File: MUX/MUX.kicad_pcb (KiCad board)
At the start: 4 copper layers, 364 x 203 mm, 139 parts, among them P1 Conn_02x36_Top_Bottom, P2 DB9_Male, P3 DB9_Male, P4 DB9_Male, P5 DB9_Male

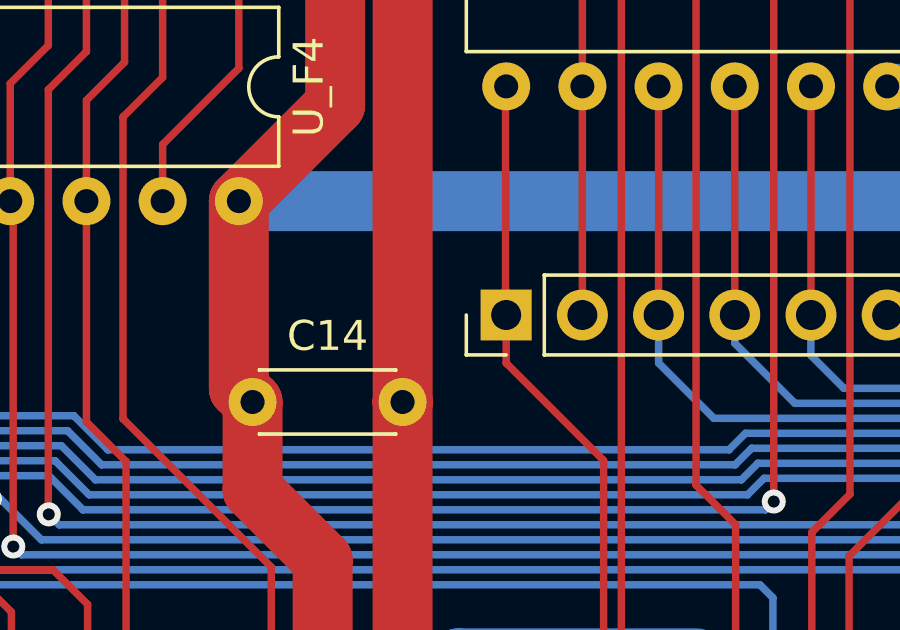
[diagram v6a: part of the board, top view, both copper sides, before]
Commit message: MUX: Some polishing
Fix up 3D model a bit, add some notes on the schematic
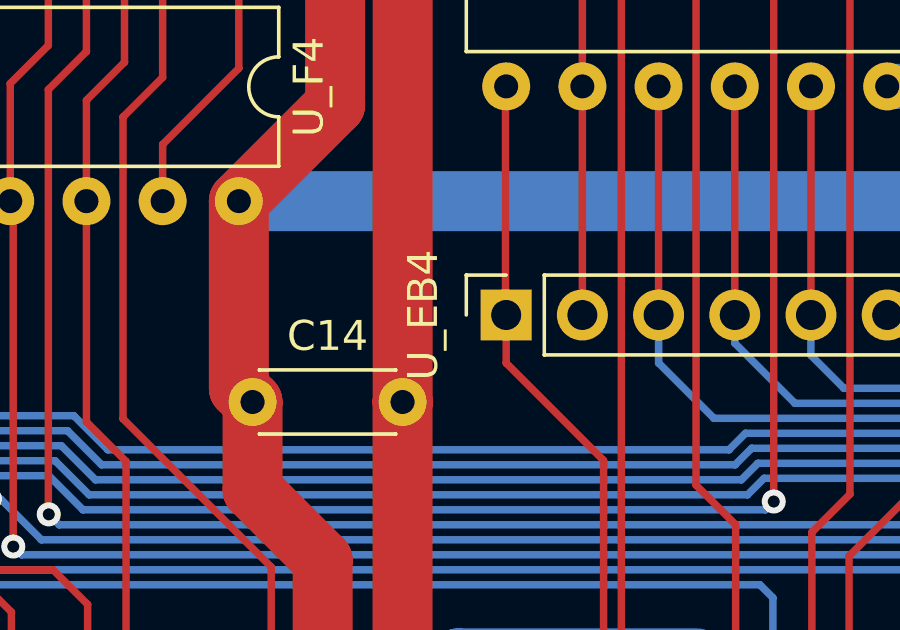
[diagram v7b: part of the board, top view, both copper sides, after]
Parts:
- U_EB4: footprint Connector_PinHeader_2.54mm:PinHeader_1x12_P2.54mm_Vertical -> Connector_PinSocket_2.54mm:PinSocket_1x12_P2.54mm_Vertical
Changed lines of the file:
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@@
     )
   )
-  (footprint "Connector_PinHeader_2.54mm:PinHeader_1x12_P2.54mm_Vertical" (layer "F.Cu")
+  (footprint "Connector_PinSocket_2.54mm:PinSocket_1x12_P2.54mm_Vertical" (layer "F.Cu")
     (at 210.790555 121.915 90)
-    (descr "Through hole straight pin header, 1x12, 2.54mm pitch, single row")
-    (tags "Through hole pin header THT 1x12 2.54mm single row")
+    (descr "Through hole straight socket strip, 1x12, 2.54mm pitch, single row (from Kicad 4.0.7), script generated")
+    (tags "Through hole socket strip THT 1x12 2.54mm single row")
     (property "Sheetfile" "MUX.kicad_sch")
     (property "Sheetname" "")
     (attr through_hole)
-    (fp_text reference "U_EB4" (at 0 -2.33 90) (layer "F.SilkS") hide
+    (fp_text reference "U_EB4" (at 0 -2.77 90) (layer "F.SilkS")
       (effects (font (size 1 1) (thickness 0.15)))
     )
-    (fp_text value "КР1533ИД3" (at -2.545 24.337245 180) (layer "F.Fab") hide
+    (fp_text value "КР1533ИД3" (at 0 30.71 90) (layer "F.Fab")
       (effects (font (size 1 1) (thickness 0.15)))
     )
-    (fp_text user "${REFERENCE}" (at 0 13.97) (layer "F.Fab")
+    (fp_text user "${REFERENCE}" (at 0 13.97 180) (layer "F.Fab")
       (effects (font (size 1 1) (thickness 0.15)))
     )
-    (fp_line (start -1.33 -1.33) (end 0 -1.33) (layer "F.SilkS") (width 0.12))
     (fp_line (start 1.33 1.27) (end 1.33 29.27) (layer "F.SilkS") (width 0.12))
+    (fp_line (start -1.33 1.27) (end -1.33 29.27) (layer "F.SilkS") (width 0.12))
     (fp_line (start -1.33 29.27) (end 1.33 29.27) (layer "F.SilkS") (width 0.12))
+    (fp_line (start 0 -1.33) (end 1.33 -1.33) (layer "F.SilkS") (width 0.12))
     (fp_line (start -1.33 1.27) (end 1.33 1.27) (layer "F.SilkS") (width 0.12))
-    (fp_line (start -1.33 0) (end -1.33 -1.33) (layer "F.SilkS") (width 0.12))
-    (fp_line (start -1.33 1.27) (end -1.33 29.27) (layer "F.SilkS") (width 0.12))
-    (fp_line (start -1.8 -1.8) (end -1.8 29.75) (layer "F.CrtYd") (width 0.05))
-    (fp_line (start -1.8 29.75) (end 1.8 29.75) (layer "F.CrtYd") (width 0.05))
-    (fp_line (start 1.8 -1.8) (end -1.8 -1.8) (layer "F.CrtYd") (width 0.05))
-    (fp_line (start 1.8 29.75) (end 1.8 -1.8) (layer "F.CrtYd") (width 0.05))
-    (fp_line (start -1.27 29.21) (end -1.27 -0.635) (layer "F.Fab") (width 0.1))
+    (fp_line (start 1.33 -1.33) (end 1.33 0) (layer "F.SilkS") (width 0.12))
+    (fp_line (start 1.75 29.7) (end -1.8 29.7) (layer "F.CrtYd") (width 0.05))
+    (fp_line (start -1.8 -1.8) (end 1.75 -1.8) (layer "F.CrtYd") (width 0.05))
+    (fp_line (start 1.75 -1.8) (end 1.75 29.7) (layer "F.CrtYd") (width 0.05))
+    (fp_line (start -1.8 29.7) (end -1.8 -1.8) (layer "F.CrtYd") (width 0.05))
+    (fp_line (start 1.27 -0.635) (end 1.27 29.21) (layer "F.Fab") (width 0.1))
+    (fp_line (start -1.27 -1.27) (end 0.635 -1.27) (layer "F.Fab") (width 0.1))
+    (fp_line (start 0.635 -1.27) (end 1.27 -0.635) (layer "F.Fab") (width 0.1))
+    (fp_line (start -1.27 29.21) (end -1.27 -1.27) (layer "F.Fab") (width 0.1))
     (fp_line (start 1.27 29.21) (end -1.27 29.21) (layer "F.Fab") (width 0.1))
-    (fp_line (start -1.27 -0.635) (end -0.635 -1.27) (layer "F.Fab") (width 0.1))
-    (fp_line (start 1.27 -1.27) (end 1.27 29.21) (layer "F.Fab") (width 0.1))
-    (fp_line (start -0.635 -1.27) (end 1.27 -1.27) (layer "F.Fab") (width 0.1))
     (pad "1" thru_hole rect (at 0 0 90) (size 1.7 1.7) (drill 1) (layers *.Cu *.Mask)
       (net 114 "/~{LoadCBR}") (pinfunction "Pin_1") (pintype "passive"))
@@
     (pad "12" thru_hole oval (at 0 27.94 90) (size 1.7 1.7) (drill 1) (layers *.Cu *.Mask)
       (net 2 "+5V") (pinfunction "Pin_12") (pintype "passive"))
-    (model "${KICAD6_3DMODEL_DIR}/Connector_PinHeader_2.54mm.3dshapes/PinHeader_1x12_P2.54mm_Vertical.wrl"
+    (model "${KICAD6_3DMODEL_DIR}/Connector_PinSocket_2.54mm.3dshapes/PinSocket_1x12_P2.54mm_Vertical.wrl"
       (offset (xyz 0 0 0))
       (scale (xyz 1 1 1))
